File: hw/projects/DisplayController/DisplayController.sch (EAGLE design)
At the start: 1 part, among them U1 AMEGA32U4"

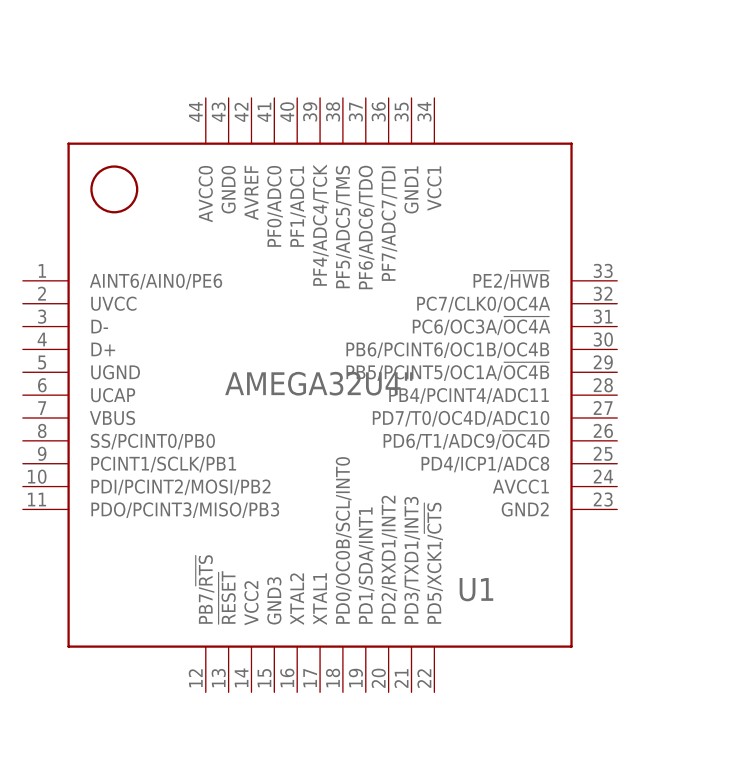
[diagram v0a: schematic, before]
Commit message: Added to the library and schematic
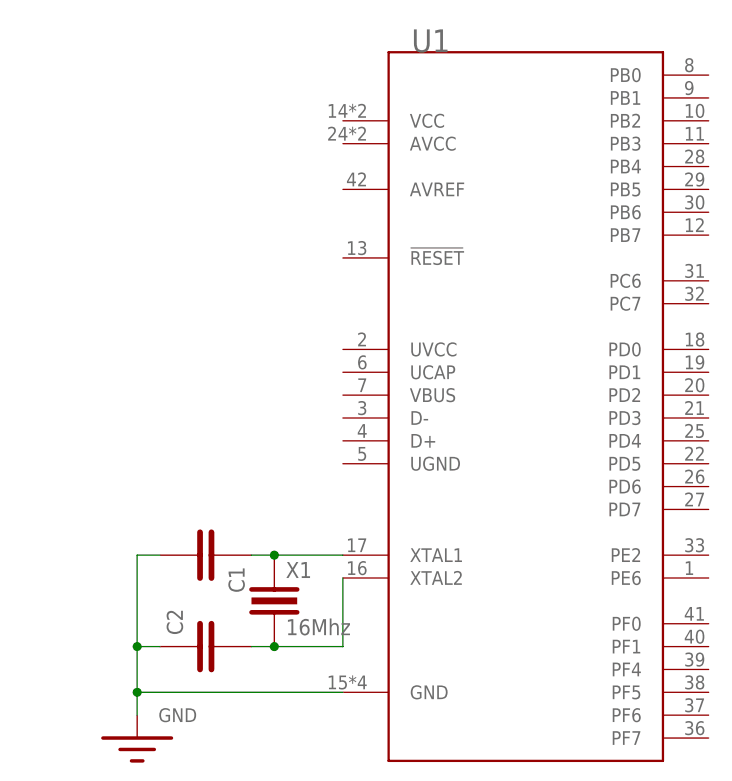
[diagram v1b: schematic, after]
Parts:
- added C1, C2: (no value), NixieDisplay:CAP-CERAMIC0805
- added X1: 16Mhz, NixieDisplay:CRYSTAL
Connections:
- new net GND: C1.2, C2.1, U1.GND
- new net N$1: C1.1, U1.XTAL1, X1.1
- new net N$2: C2.2, U1.XTAL2, X1.2
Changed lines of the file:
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@@
 <parts>
 <part name="U1" library="NixieDisplay" deviceset="AMEGA32U4" device="&quot;"/>
+<part name="X1" library="NixieDisplay" deviceset="CRYSTAL" device="" value="16Mhz"/>
+<part name="C1" library="NixieDisplay" deviceset="CAP-CERAMIC" device="0805"/>
+<part name="C2" library="NixieDisplay" deviceset="CAP-CERAMIC" device="0805"/>
+<part name="GND1" library="NixieDisplay" deviceset="GND" device=""/>
 </parts>
 <sheets>
@@
 <instances>
 <instance part="U1" gate="G$1" x="99.06" y="53.34" smashed="yes">
-<attribute name="NAME" x="91.44" y="30.48" size="2.54" layer="95"/>
-<attribute name="VALUE" x="76.2" y="53.34" size="2.54" layer="96" align="bottom-center"/>
+<attribute name="NAME" x="86.36" y="91.44" size="2.54" layer="95"/>
 </instance>
+<instance part="X1" gate="G$1" x="71.12" y="30.48" smashed="yes">
+<attribute name="NAME" x="72.39" y="33.02" size="1.778" layer="95"/>
+<attribute name="VALUE" x="72.39" y="26.67" size="1.778" layer="96"/>
+</instance>
+<instance part="C1" gate="G$1" x="63.5" y="35.56" smashed="yes" rot="R270">
+<attribute name="NAME" x="66.04" y="34.29" size="1.778" layer="95" rot="R270"/>
+<attribute name="VALUE" x="59.69" y="34.29" size="1.778" layer="96" rot="R270"/>
+</instance>
+<instance part="C2" gate="G$1" x="63.5" y="25.4" smashed="yes" rot="R90">
+<attribute name="NAME" x="60.96" y="26.67" size="1.778" layer="95" rot="R90"/>
+<attribute name="VALUE" x="67.31" y="26.67" size="1.778" layer="96" rot="R90"/>
+</instance>
+<instance part="GND1" gate="G$1" x="55.88" y="17.78" smashed="yes"/>
 </instances>
 <busses>
 </busses>
 <nets>
+<net name="N$1" class="0">
+<segment>
+<pinref part="U1" gate="G$1" pin="XTAL1"/>
+<pinref part="C1" gate="G$1" pin="1"/>
+<wire x1="78.74" y1="35.56" x2="71.12" y2="35.56" width="0.1524" layer="91"/>
+<pinref part="X1" gate="G$1" pin="1"/>
+<wire x1="71.12" y1="35.56" x2="68.58" y2="35.56" width="0.1524" layer="91"/>
+<junction x="71.12" y="35.56"/>
+</segment>
+</net>
+<net name="N$2" class="0">
+<segment>
+<pinref part="U1" gate="G$1" pin="XTAL2"/>
+<pinref part="X1" gate="G$1" pin="2"/>
+<wire x1="78.74" y1="33.02" x2="78.74" y2="25.4" width="0.1524" layer="91"/>
+<wire x1="78.74" y1="25.4" x2="71.12" y2="25.4" width="0.1524" layer="91"/>
+<pinref part="C2" gate="G$1" pin="2"/>
+<wire x1="68.58" y1="25.4" x2="71.12" y2="25.4" width="0.1524" layer="91"/>
+<junction x="71.12" y="25.4"/>
+</segment>
+</net>
+<net name="GND" class="0">
+<segment>
+<pinref part="C1" gate="G$1" pin="2"/>
+<wire x1="58.42" y1="35.56" x2="55.88" y2="35.56" width="0.1524" layer="91"/>
+<wire x1="55.88" y1="35.56" x2="55.88" y2="25.4" width="0.1524" layer="91"/>
+<pinref part="U1" gate="G$1" pin="GND"/>
+<wire x1="55.88" y1="25.4" x2="55.88" y2="20.32" width="0.1524" layer="91"/>
+<wire x1="55.88" y1="20.32" x2="78.74" y2="20.32" width="0.1524" layer="91"/>
+<pinref part="C2" gate="G$1" pin="1"/>
+<wire x1="58.42" y1="25.4" x2="55.88" y2="25.4" width="0.1524" layer="91"/>
+<junction x="55.88" y="25.4"/>
+<wire x1="55.88" y1="20.32" x2="55.88" y2="17.78" width="0.1524" layer="91"/>
+<junction x="55.88" y="20.32"/>
+<pinref part="GND1" gate="G$1" pin="GND"/>
+</segment>
+</net>
 </nets>
 </sheet>

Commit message: Added a lot to library
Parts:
- added C3: (no value), NixieDisplay:CAP-CERAMIC0805
- added R1, R2: (no value), NixieDisplay:RESISTOR0805
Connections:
- new net +5V: U1.AVCC, U1.AVREF, U1.UVCC, U1.VBUS, U1.VCC
- new net N$4: C3.1, U1.UCAP
- net GND: now also C3.2, U1.UGND

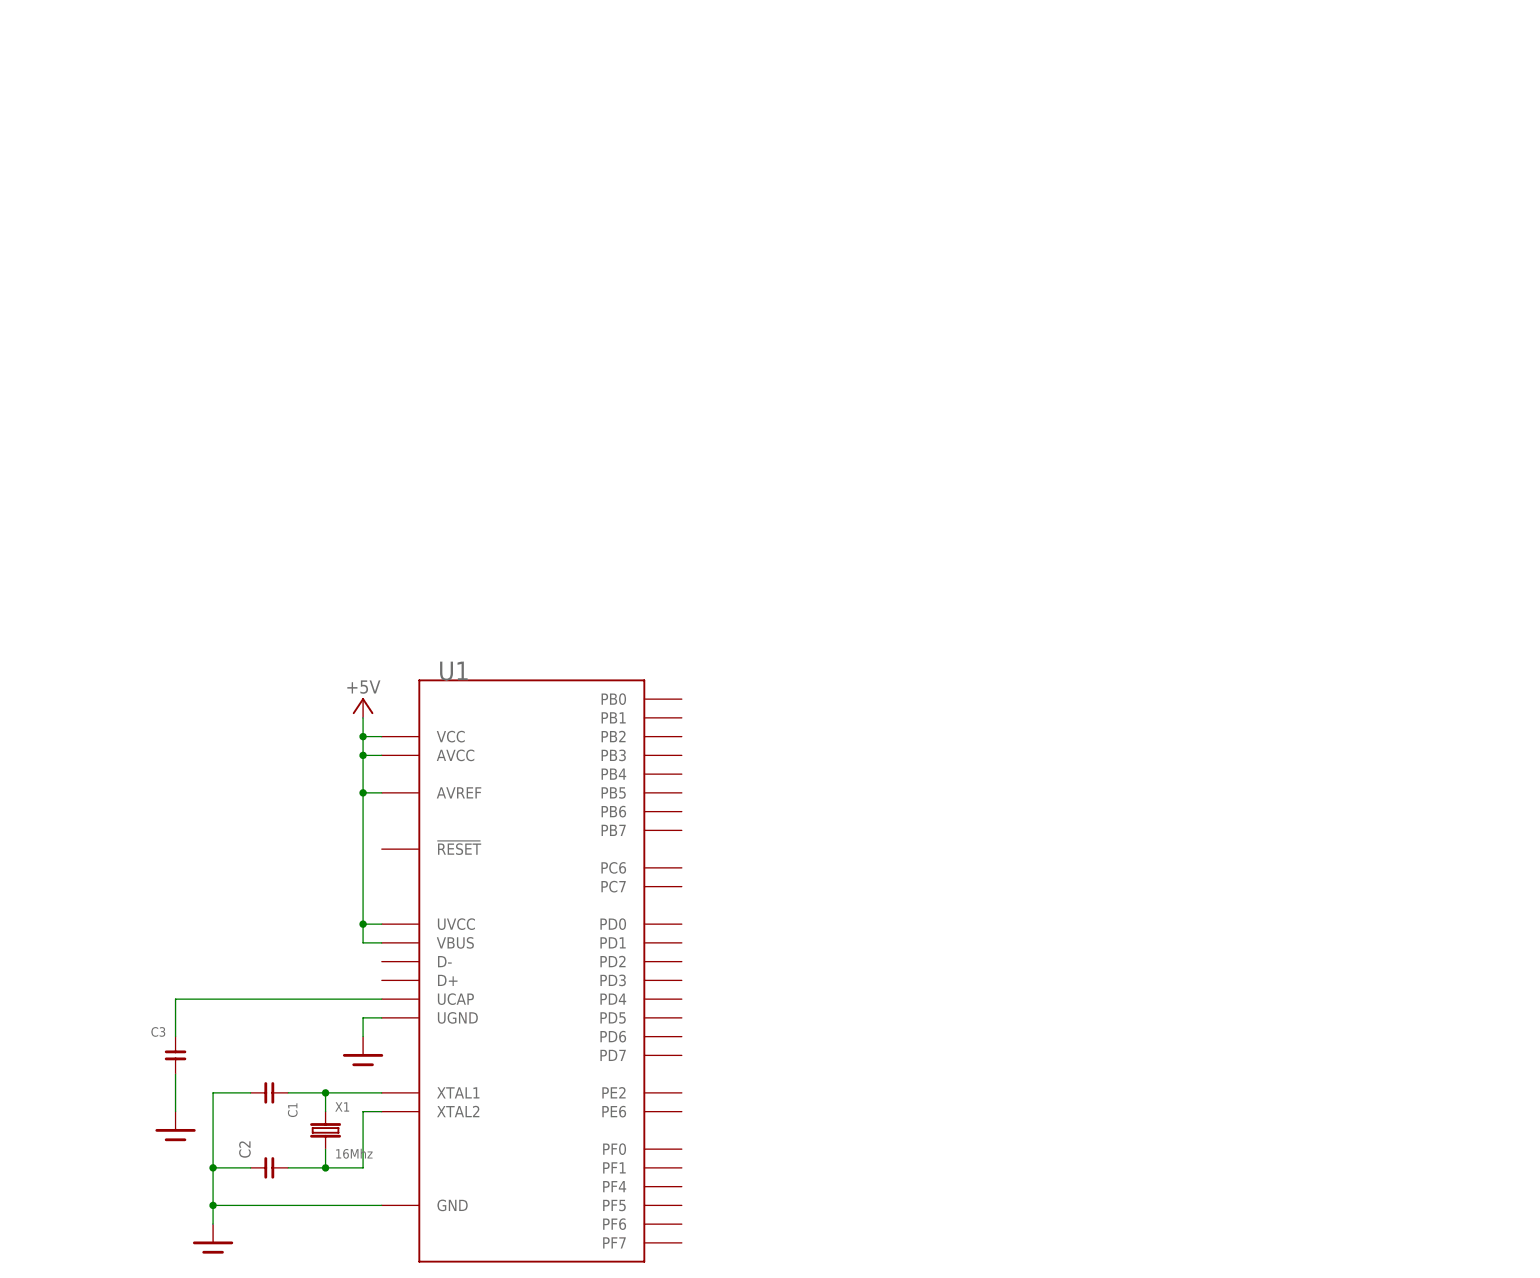
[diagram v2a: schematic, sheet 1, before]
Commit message: added lots of io and regulation
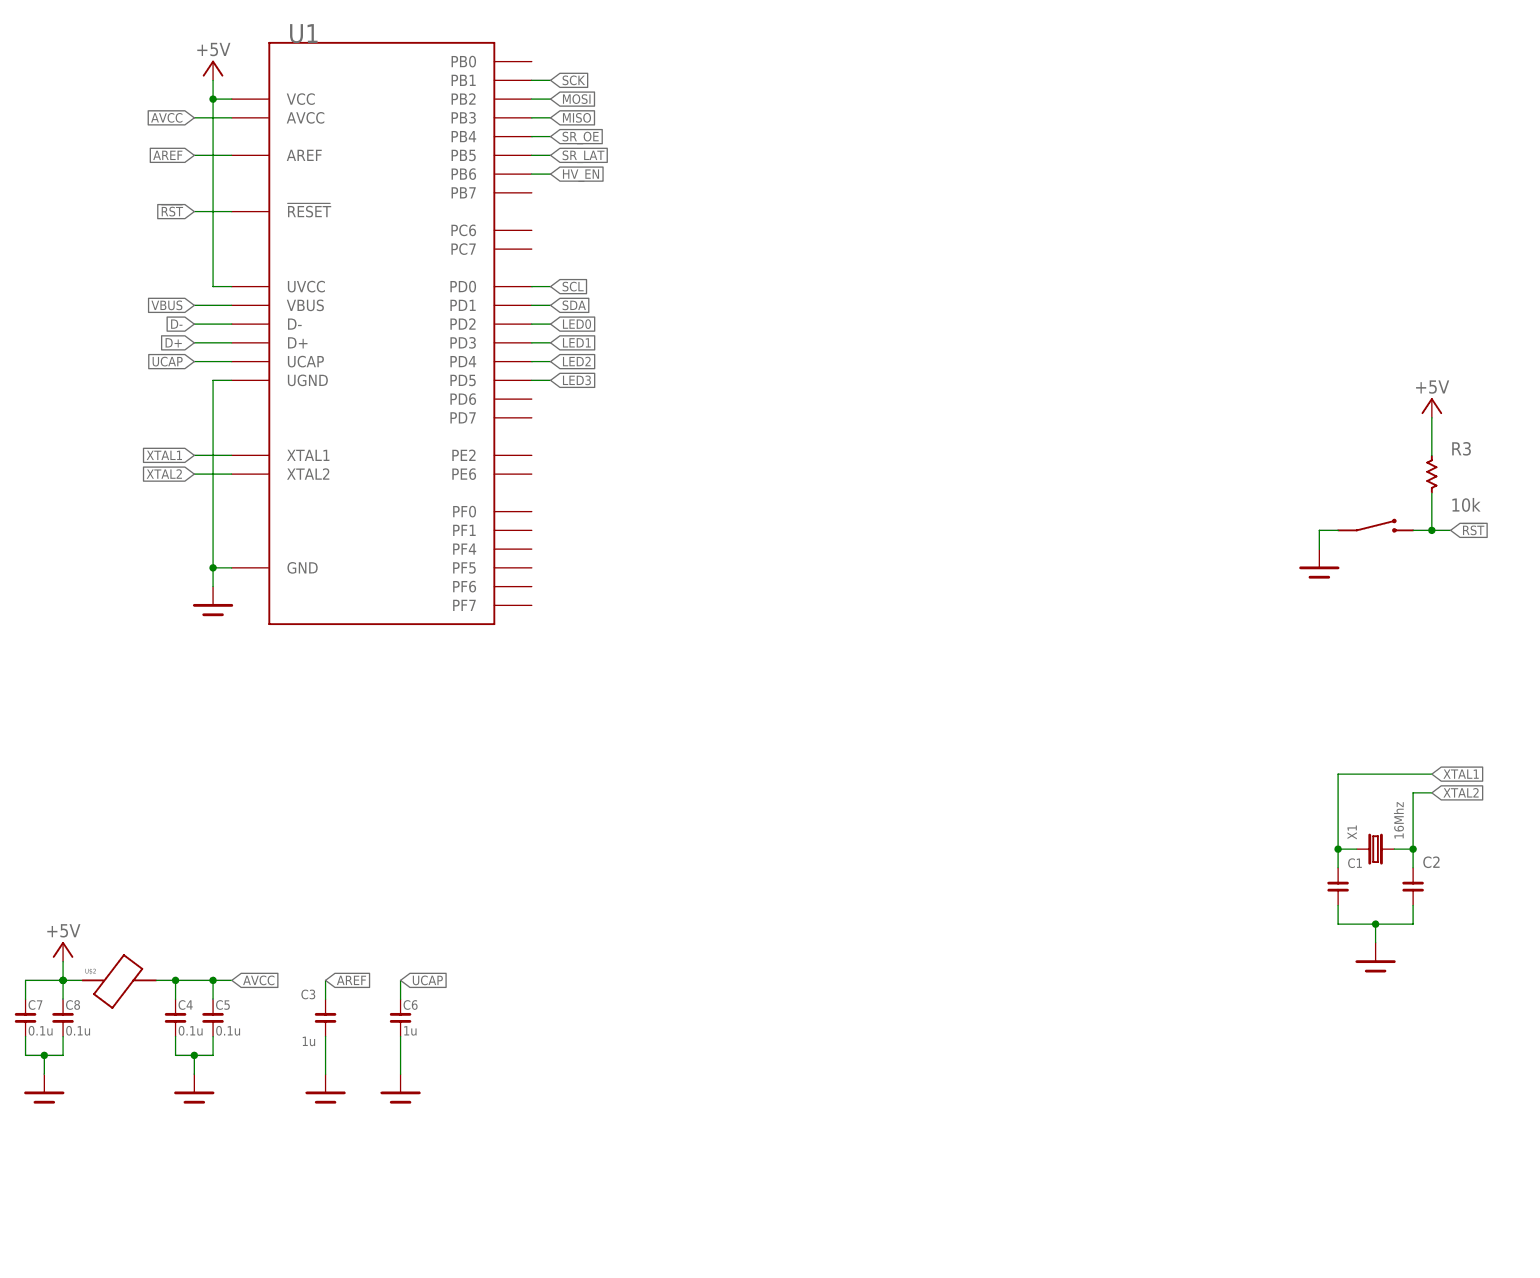
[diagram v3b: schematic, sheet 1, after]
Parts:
- added C4, C5, C7, C8: 0.1u, NixieDisplay:CAP-CERAMIC0805
- added C6: 1u, NixieDisplay:CAP-CERAMIC0805
- added C9: (no value), NixieDisplay:CAP-CERAMIC0805
- added D1: (no value), NixieDisplay:DIODE-SCHOTTKY-DO-214AC
- added D2, D3, D4, D5: LTST-C150GKT, NixieDisplay:LTST-C150GKT
- added J1: B4B-EH-A, NixieDisplay:B4B-EH-A
- added J2: JST-SH-8, NixieDisplay:JST-SH-8
- added L1: (no value), NixieDisplay:INDUCTOR-7447779168
- added R3: 10k, NixieDisplay:RESISTOR0805
- added R4, R5, R6, R7: (no value), NixieDisplay:RESISTOR0805
- added U$1: SWITCH-SPST, NixieDisplay:SWITCH-SPST
- added U$2: FERRITE, NixieDisplay:FERRITE
- added U2: LM2675-5.0, NixieDisplay:LM2675-5.0
- C3: value (none) -> 1u
- R1, R2: value (none) -> 22
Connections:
- net N$1 renamed XTAL1
- new net !RST: R3.2, U$1.P$2, U1.!RESET
- new net +12V: J2.8, U2.VIN
- new net AREF: C3.1, U1.AREF
- new net AVCC: C4.1, C5.1, U$2.P$2, U1.AVCC
- new net D+: R1.2, U1.D+
- new net D-: R2.2, U1.D-
- new net HV_EN: J2.2, U1.PB6
- new net LED0: R4.1, U1.PD2
- new net LED1: R5.1, U1.PD3
- new net LED2: R6.1, U1.PD4
- new net LED3: R7.1, U1.PD5
- new net MISO: U1.PB3
- new net MOSI: J2.5, U1.PB2
- new net N$1: J1.3, R1.1
- new net N$10: D4.A, R6.2
- new net N$12: D5.A, R7.2
- new net N$3: D2.A, R4.2
- new net N$5: C9.1, U2.CB
- new net N$8: D3.A, R5.2
- new net SCK: J2.6, U1.PB1
- new net SCL: U1.PD0
- new net SDA: U1.PD1
- new net SR_LAT: J2.3, U1.PB5
- new net SR_OE: J2.4, U1.PB4
- new net UCAP: C6.1, U1.UCAP
- new net VBUS: J1.4, U1.VBUS
- new net XTAL2: C2.1, U1.XTAL2, X1.2
- net +5V: now also C7.1, C8.1, J2.7, L1.1, R3.1, U$2.P$1, U2.FB; no longer U1.AVCC, U1.AVREF, U1.VBUS
- net GND: now also C2.2, C4.2, C5.2, C6.2, C7.2, C8.2, D1.A, D2.C, D3.C, D4.C, D5.C, J1.1, J2.1, J2.MNT1, J2.MNT2, U$1.P$1, U2.GND; no longer C2.1
- net N$2: now also J1.2, R2.1; no longer C2.2, U1.XTAL2, X1.2
- net N$4: now also C9.2, D1.C, L1.2, U2.VSW; no longer C3.1, U1.UCAP
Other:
- moved on the sheet: C1, C2, C3, U1, X1

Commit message: progress on controller board, started driver
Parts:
- added C10, C11: (no value), NixieDisplay:CAP-CERAMIC0805
- added J3, J4, J5, J6: JST-SH-2, NixieDisplay:JST-SH-2
- added R10, R11, R8, R9: (no value), NixieDisplay:RESISTOR0805
- added U$3, U$4, U$5, U$6: SWITCH-SPST, NixieDisplay:SWITCH-SPST
- added U$7: 32.768kHz, NixieDisplay:TUNING_FORK
- added U$8: MCP7940N, NixieDisplay:MCP7940N
- added U3: TPS73633-DCQ, NixieDisplay:TPS73633-DCQ
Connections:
- new net N$14: U1.PE6
- new net N$6: C10.1, U$7.2, U$8.X1
- new net N$7: C11.1, U$7.1, U$8.X2
- new net RTC_MFP: U$8.MFP, U1.PB7
- new net SW0: J3.1, R8.2, U$3.P$1, U1.PF0
- new net SW1: J4.1, R9.2, U$4.P$1, U1.PF1
- new net SW2: J5.1, R10.2, U$5.P$1, U1.PF4
- new net SW3: J6.1, R11.2, U$6.P$1, U1.PF5
- net +5V: now also R10.1, R11.1, R8.1, R9.1, U$8.VCC
- net GND: now also C10.2, C11.2, J3.2, J3.M1, J3.M2, J4.2, J4.M1, J4.M2, J5.2, J5.M1, J5.M2, J6.2, J6.M1, J6.M2, U$3.P$2, U$4.P$2, U$5.P$2, U$6.P$2, U$7.P$1, U$8.VSS
- net SCL: now also U$8.SCL
- net SDA: now also U$8.SDA
